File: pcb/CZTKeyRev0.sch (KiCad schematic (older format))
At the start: 195 parts, among them U1 proton_c

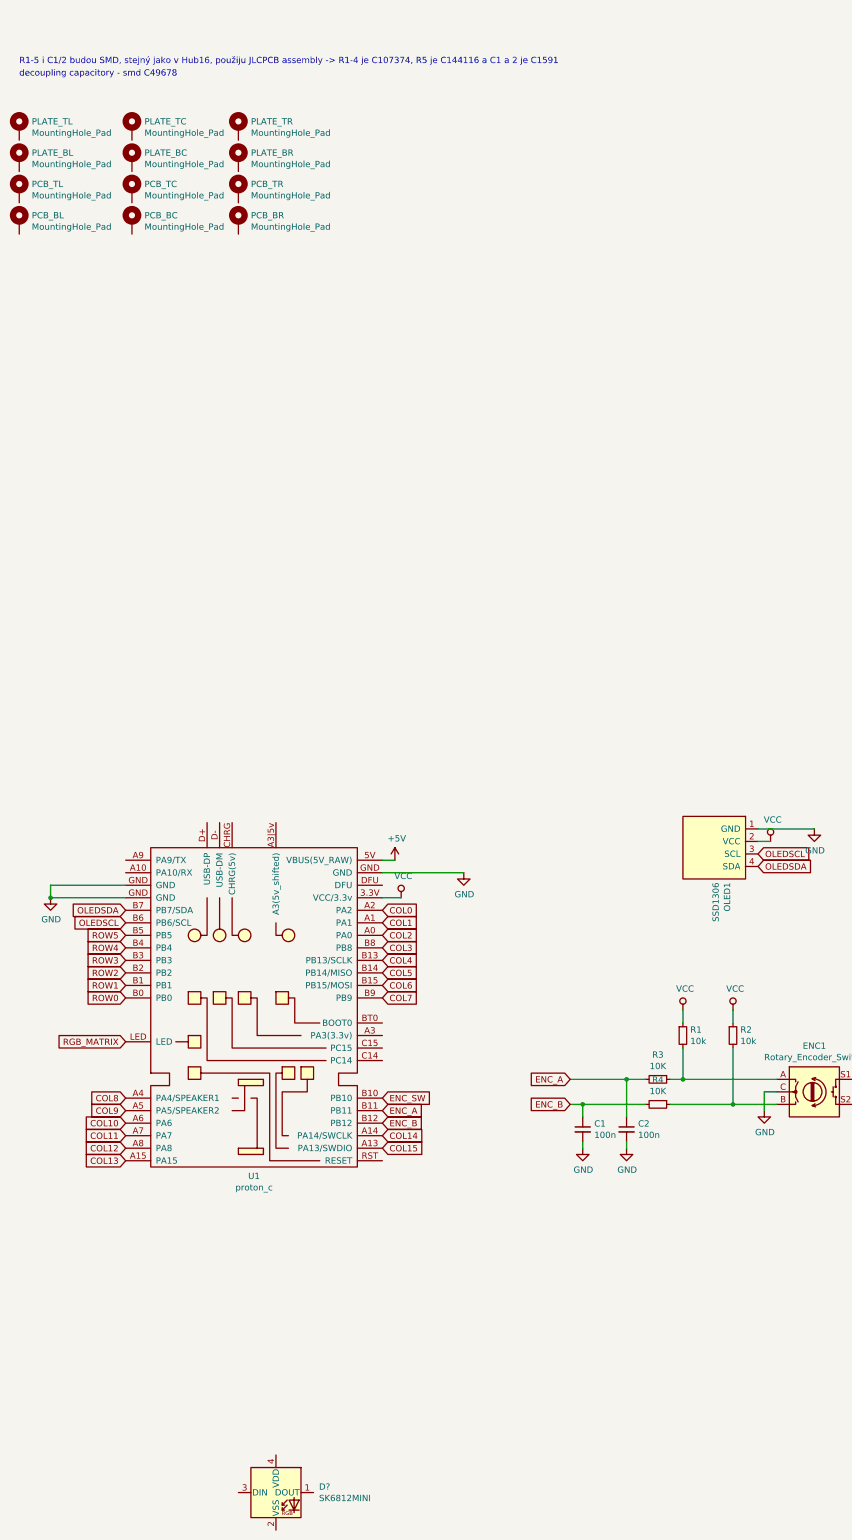
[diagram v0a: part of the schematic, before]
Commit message: Added the IC for ext 5v and led data
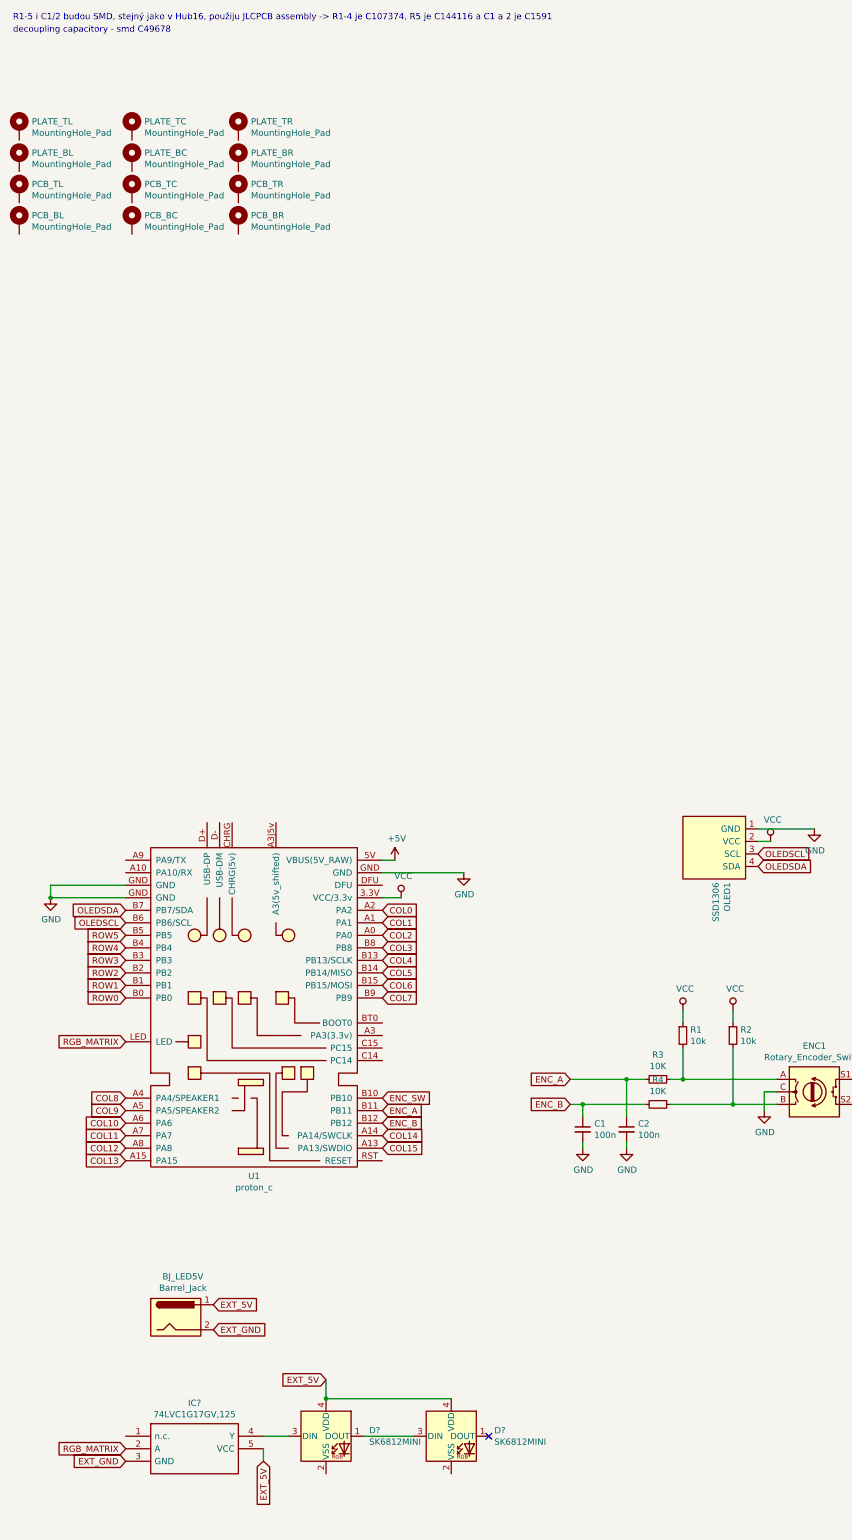
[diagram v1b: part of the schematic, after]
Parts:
- added BJ_LED5V: Barrel_Jack, symbol Connector:Barrel_Jack
- added D?: SK6812MINI, LED_SMD:LED_SK6812MINI_PLCC4_3.5x3.5mm_P1.75mm, symbol LED:SK6812MINI
- added IC?: 74LVC1G17GV,125, SOT95P275X110-5N, symbol SamacSys_Parts:74LVC1G17GV,125
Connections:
- net RGB_MATRIX: now also IC?.2 (A)
- net at D?.1 (DOUT): now also D?.3 (DIN)
- net at D?.3 (DIN): now also IC?.4 (Y)
- net EXT_5V: now reaches D?.4 (VDD)
- net EXT_5V: now also BJ_LED5V.1, D?.4 (VDD), IC?.5 (VCC)
- new net EXT_GND: BJ_LED5V.2, IC?.3 (GND)
- no-connect marks 0 -> 1
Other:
- moved on the sheet: D?
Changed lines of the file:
@@
 Text GLabel 1450 7950 0    50   Input ~ 0
 RGB_MATRIX
-Text Notes 600  150  0    50   ~ 0
+Text Notes 550  -200 0    50   ~ 0
 R1-5 i C1/2 budou SMD, stejný jako v Hub16, použiju JLCPCB assembly -> R1-4 je C107374, R5 je C144116 a C1 a 2 je C1591
 Text GLabel 3500 8500 2    50   Input ~ 0
@@
 Text GLabel 12200 9150 2    50   Input ~ 0
 ENC_S2
-Text Notes 600  250  0    50   ~ 0
+Text Notes 550  -100 0    50   ~ 0
 decoupling capacitory - smd C49678
 Wire Wire Line
@@
 $EndComp
 $Comp
+L Connector:Barrel_Jack BJ_LED5V
+U 1 1 5FC7DC4D
+P 1850 10150
+F 0 "BJ_LED5V" H 1907 10475 50  0000 C CNN
+F 1 "Barrel_Jack" H 1907 10384 50  0000 C CNN
+F 2 "" H 1900 10110 50  0001 C CNN
+F 3 "~" H 1900 10110 50  0001 C CNN
+	1    1850 10150
+	1    0    0    -1
+$EndComp
+Text GLabel 1450 11200 0    50   Input ~ 0
+RGB_MATRIX
+$Comp
+L LED:SK6812MINI D?
+U 1 1 5FC81A59
+P 4050 11100
+F 0 "D?" H 4394 11146 50  0000 L CNN
+F 1 "SK6812MINI" H 4394 11055 50  0000 L CNN
+F 2 "LED_SMD:LED_SK6812MINI_PLCC4_3.5x3.5mm_P1.75mm" H 4100 10800 50  0001 L TNN
+F 3 "https://cdn-shop.adafruit.com/product-files/2686/SK6812MINI_REV.01-1-2.pdf" H 4150 10725 50  0001 L TNN
+	1    4050 11100
+	1    0    0    -1
+$EndComp
+NoConn ~ 4350 11100
+Text GLabel 2150 10050 2    50   Input ~ 0
+EXT_5V
+Text GLabel 2150 10250 2    50   Input ~ 0
+EXT_GND
+Text GLabel 1450 11300 0    50   Input ~ 0
+EXT_GND
+Text GLabel 2550 11300 3    50   Input ~ 0
+EXT_5V
+$Comp
 L LED:SK6812MINI D?
 U 1 1 5FCBCA87
-P 2650 11550
-F 0 "D?" H 2994 11596 50  0000 L CNN
-F 1 "SK6812MINI" H 2994 11505 50  0000 L CNN
-F 2 "LED_SMD:LED_SK6812MINI_PLCC4_3.5x3.5mm_P1.75mm" H 2700 11250 50  0001 L TNN
-F 3 "https://cdn-shop.adafruit.com/product-files/2686/SK6812MINI_REV.01-1-2.pdf" H 2750 11175 50  0001 L TNN
-	1    2650 11550
-	1    0    0    -1
-$EndComp
+P 3050 11100
+F 0 "D?" H 3394 11146 50  0000 L CNN
+F 1 "SK6812MINI" H 3394 11055 50  0000 L CNN
+F 2 "LED_SMD:LED_SK6812MINI_PLCC4_3.5x3.5mm_P1.75mm" H 3100 10800 50  0001 L TNN
+F 3 "https://cdn-shop.adafruit.com/product-files/2686/SK6812MINI_REV.01-1-2.pdf" H 3150 10725 50  0001 L TNN
+	1    3050 11100
+	1    0    0    -1
+$EndComp
+$Comp
+L SamacSys_Parts:74LVC1G17GV,125 IC?
+U 1 1 5FEEF888
+P 1450 11100
+F 0 "IC?" H 2000 11365 50  0000 C CNN
+F 1 "74LVC1G17GV,125" H 2000 11274 50  0000 C CNN
+F 2 "SOT95P275X110-5N" H 2400 11200 50  0001 L CNN
+F 3 "https://assets.nexperia.com/documents/data-sheet/74LVC1G17.pdf" H 2400 11100 50  0001 L CNN
+F 4 "74LVC1G17 - Single Schmitt trigger buffer@en-us" H 2400 11000 50  0001 L CNN "Description"
+F 5 "1.1" H 2400 10900 50  0001 L CNN "Height"
+F 6 "771-LVC1G17GV125" H 2400 10800 50  0001 L CNN "Mouser Part Number"
+F 7 "https://www.mouser.co.uk/ProductDetail/Nexperia/74LVC1G17GV125?qs=me8TqzrmIYX3DxU5Fpa8sQ%3D%3D" H 2400 10700 50  0001 L CNN "Mouser Price/Stock"
+F 8 "Nexperia" H 2400 10600 50  0001 L CNN "Manufacturer_Name"
+F 9 "74LVC1G17GV,125" H 2400 10500 50  0001 L CNN "Manufacturer_Part_Number"
+	1    1450 11100
+	1    0    0    -1
+$EndComp
+Wire Wire Line
+	2550 11100 2750 11100
+Wire Wire Line
+	2550 11200 2550 11300
+Wire Wire Line
+	3350 11100 3750 11100
+Text GLabel 3050 10650 0    50   Input ~ 0
+EXT_5V
+Wire Wire Line
+	3050 10650 3050 10800
+Wire Wire Line
+	4050 10800 3050 10800
+Connection ~ 3050 10800
 $EndSCHEMATC

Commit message: Organizing lib, gerber and schematic pdf files into subfolders
Its for easier navigation
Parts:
- removed C1, C2: 100n, Capacitor_SMD:C_0603_1608Metric, symbol Device:C_Small
- removed D? (x2): SK6812MINI, LED_SMD:LED_SK6812MINI_PLCC4_3.5x3.5mm_P1.75mm, symbol LED:SK6812MINI
- removed R1, R2: 10k, Resistor_SMD:R_Array_Convex_4x0603, symbol Device:R_Small
- removed R3, R4: 10K, Resistor_SMD:R_Array_Convex_4x0603, symbol Device:R_Small
- added LED1, LED10, LED11, LED12, LED13, LED14, LED15, LED16, LED17, LED18, LED19, LED2, LED20, LED21, LED22, LED23, LED24, LED25, LED26, LED27, LED28, LED29, LED3, LED30, LED31, LED32, LED33, LED34, LED35, LED36, LED37, LED38, LED39, LED4, LED40, LED41, LED42, LED43, LED44, LED45, LED46, LED47, LED48, LED49, LED5, LED50, LED51, LED52, LED53, LED54, LED55, LED56, LED57, LED58, LED59, LED6, LED60, LED61, LED62, LED63, LED64, LED65, LED66, LED67, LED68, LED69, LED7, LED70, LED71, LED72, LED73, LED74, LED75, LED76, LED77, LED78, LED79, LED8, LED80, LED81, LED82, LED83, LED84, LED85, LED86, LED87, LED9: YS-SK6812MINI-E, rgb led reverse mount:SK6812MINIE-simple, symbol kbd:YS-SK6812MINI-E
- EXT_IC1: renamed from IC?; footprint SOT95P275X110-5N -> SamacSys_Parts:SOT95P275X110-5N
- PCB_BC1: renamed from PCB_BC; footprint (none) -> MountingHole:MountingHole_2.2mm_M2_Pad
- PCB_BL1: renamed from PCB_BL; footprint (none) -> MountingHole:MountingHole_2.2mm_M2_Pad
- PCB_BR1: renamed from PCB_BR; footprint (none) -> MountingHole:MountingHole_2.2mm_M2_Pad
- PCB_TC1: renamed from PCB_TC; footprint (none) -> MountingHole:MountingHole_2.2mm_M2_Pad
- PCB_TL1: renamed from PCB_TL; footprint (none) -> MountingHole:MountingHole_2.2mm_M2_Pad
- PCB_TR1: renamed from PCB_TR; footprint (none) -> MountingHole:MountingHole_2.2mm_M2_Pad
- PLATE_BC1: renamed from PLATE_BC; footprint (none) -> MountingHole:MountingHole_2.2mm_M2_Pad
- PLATE_BL1: renamed from PLATE_BL; footprint (none) -> MountingHole:MountingHole_2.2mm_M2_Pad
- PLATE_BR1: renamed from PLATE_BR; footprint (none) -> MountingHole:MountingHole_2.2mm_M2_Pad
- PLATE_TC1: renamed from PLATE_TC; footprint (none) -> MountingHole:MountingHole_2.2mm_M2_Pad
- PLATE_TL1: renamed from PLATE_TL; footprint (none) -> MountingHole:MountingHole_2.2mm_M2_Pad
- PLATE_TR1: renamed from PLATE_TR; footprint (none) -> MountingHole:MountingHole_2.2mm_M2_Pad
- renumbered BJ_LED5V to BJ_LED5V1, D87 to D0
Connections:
- net +5V: now also OLED1.2 (VCC)
- net COL0: now also ENC1.S1
- net COL4: no longer ENC1.S1
- net ENC_A: now also ENC1.A
- net ENC_B: now also ENC1.B
- net EXT_5V: now also LED1.1 (VDD), LED10.1 (VDD), LED11.1 (VDD), LED12.1 (VDD), LED13.1 (VDD), LED14.1 (VDD), LED15.1 (VDD), LED16.1 (VDD), LED17.1 (VDD), LED18.1 (VDD), LED19.1 (VDD), LED2.1 (VDD), LED20.1 (VDD), LED21.1 (VDD), LED22.1 (VDD), LED23.1 (VDD), LED24.1 (VDD), LED25.1 (VDD), LED26.1 (VDD), LED27.1 (VDD), LED28.1 (VDD), LED29.1 (VDD), LED3.1 (VDD), LED30.1 (VDD), LED31.1 (VDD), LED32.1 (VDD), LED33.1 (VDD), LED34.1 (VDD), LED35.1 (VDD), LED36.1 (VDD), LED37.1 (VDD), LED38.1 (VDD), LED39.1 (VDD), LED4.1 (VDD), LED40.1 (VDD), LED41.1 (VDD), LED42.1 (VDD), LED43.1 (VDD), LED44.1 (VDD), LED45.1 (VDD), LED46.1 (VDD), LED47.1 (VDD), LED48.1 (VDD), LED49.1 (VDD), LED5.1 (VDD), LED50.1 (VDD), LED51.1 (VDD), LED52.1 (VDD), LED53.1 (VDD), LED54.1 (VDD), LED55.1 (VDD), LED56.1 (VDD), LED57.1 (VDD), LED58.1 (VDD), LED59.1 (VDD), LED6.1 (VDD), LED60.1 (VDD), LED61.1 (VDD), LED62.1 (VDD), LED63.1 (VDD), LED64.1 (VDD), LED65.1 (VDD), LED66.1 (VDD), LED67.1 (VDD), LED68.1 (VDD), LED69.1 (VDD), LED7.1 (VDD), LED70.1 (VDD), LED71.1 (VDD), LED72.1 (VDD), LED73.1 (VDD), LED74.1 (VDD), LED75.1 (VDD), LED76.1 (VDD), LED77.1 (VDD), LED78.1 (VDD), LED79.1 (VDD), LED8.1 (VDD), LED80.1 (VDD), LED81.1 (VDD), LED82.1 (VDD), LED83.1 (VDD), LED84.1 (VDD), LED85.1 (VDD), LED86.1 (VDD), LED87.1 (VDD), LED9.1 (VDD)
- net EXT_GND: now also LED1.3 (VSS), LED10.3 (VSS), LED11.3 (VSS), LED12.3 (VSS), LED13.3 (VSS), LED14.3 (VSS), LED15.3 (VSS), LED16.3 (VSS), LED17.3 (VSS), LED18.3 (VSS), LED19.3 (VSS), LED2.3 (VSS), LED20.3 (VSS), LED21.3 (VSS), LED22.3 (VSS), LED23.3 (VSS), LED24.3 (VSS), LED25.3 (VSS), LED26.3 (VSS), LED27.3 (VSS), LED28.3 (VSS), LED29.3 (VSS), LED3.3 (VSS), LED30.3 (VSS), LED31.3 (VSS), LED32.3 (VSS), LED33.3 (VSS), LED34.3 (VSS), LED35.3 (VSS), LED36.3 (VSS), LED37.3 (VSS), LED38.3 (VSS), LED39.3 (VSS), LED4.3 (VSS), LED40.3 (VSS), LED41.3 (VSS), LED42.3 (VSS), LED43.3 (VSS), LED44.3 (VSS), LED45.3 (VSS), LED46.3 (VSS), LED47.3 (VSS), LED48.3 (VSS), LED49.3 (VSS), LED5.3 (VSS), LED50.3 (VSS), LED51.3 (VSS), LED52.3 (VSS), LED53.3 (VSS), LED54.3 (VSS), LED55.3 (VSS), LED56.3 (VSS), LED57.3 (VSS), LED58.3 (VSS), LED59.3 (VSS), LED6.3 (VSS), LED60.3 (VSS), LED61.3 (VSS), LED62.3 (VSS), LED63.3 (VSS), LED64.3 (VSS), LED65.3 (VSS), LED66.3 (VSS), LED67.3 (VSS), LED68.3 (VSS), LED69.3 (VSS), LED7.3 (VSS), LED70.3 (VSS), LED71.3 (VSS), LED72.3 (VSS), LED73.3 (VSS), LED74.3 (VSS), LED75.3 (VSS), LED76.3 (VSS), LED77.3 (VSS), LED78.3 (VSS), LED79.3 (VSS), LED8.3 (VSS), LED80.3 (VSS), LED81.3 (VSS), LED82.3 (VSS), LED83.3 (VSS), LED84.3 (VSS), LED85.3 (VSS), LED86.3 (VSS), LED87.3 (VSS), LED9.3 (VSS)
- net ROW0: now also D0.1 (K)
- net ROW5: no longer D0.1 (K)
- net VCC: no longer OLED1.2 (VCC)
- net at EXT_IC1.4 (Y): now also LED1.4 (DIN)
- net ENC_SW: no longer names the net of U1.B10 (PB10)
- new net: LED1.2 (DOUT), LED2.4 (DIN)
- new net: LED2.2 (DOUT), LED3.4 (DIN)
- new net: LED3.2 (DOUT), LED4.4 (DIN)
- new net: LED4.2 (DOUT), LED5.4 (DIN)
- new net: LED5.2 (DOUT), LED6.4 (DIN)
- new net: LED6.2 (DOUT), LED7.4 (DIN)
- new net: LED7.2 (DOUT), LED8.4 (DIN)
- new net: LED8.2 (DOUT), LED9.4 (DIN)
- new net: LED10.4 (DIN), LED9.2 (DOUT)
- new net: LED10.2 (DOUT), LED11.4 (DIN)
- new net: LED11.2 (DOUT), LED12.4 (DIN)
- new net: LED12.2 (DOUT), LED13.4 (DIN)
- new net: LED13.2 (DOUT), LED14.4 (DIN)
- new net: LED14.2 (DOUT), LED30.4 (DIN)
- new net: LED29.4 (DIN), LED30.2 (DOUT)
- new net: LED28.4 (DIN), LED29.2 (DOUT)
- new net: LED27.4 (DIN), LED28.2 (DOUT)
- new net: LED26.4 (DIN), LED27.2 (DOUT)
- new net: LED25.4 (DIN), LED26.2 (DOUT)
- new net: LED24.4 (DIN), LED25.2 (DOUT)
- new net: LED23.4 (DIN), LED24.2 (DOUT)
- new net: LED22.4 (DIN), LED23.2 (DOUT)
- new net: LED21.4 (DIN), LED22.2 (DOUT)
- new net: LED20.4 (DIN), LED21.2 (DOUT)
- new net: LED19.4 (DIN), LED20.2 (DOUT)
- new net: LED18.4 (DIN), LED19.2 (DOUT)
- new net: LED17.4 (DIN), LED18.2 (DOUT)
- new net: LED16.4 (DIN), LED17.2 (DOUT)
- new net: LED15.4 (DIN), LED16.2 (DOUT)
- new net: LED15.2 (DOUT), LED31.4 (DIN)
- new net: LED31.2 (DOUT), LED32.4 (DIN)
- new net: LED32.2 (DOUT), LED33.4 (DIN)
- new net: LED33.2 (DOUT), LED34.4 (DIN)
- new net: LED34.2 (DOUT), LED35.4 (DIN)
- new net: LED35.2 (DOUT), LED36.4 (DIN)
- new net: LED36.2 (DOUT), LED37.4 (DIN)
- new net: LED37.2 (DOUT), LED38.4 (DIN)
- new net: LED38.2 (DOUT), LED39.4 (DIN)
- new net: LED39.2 (DOUT), LED40.4 (DIN)
- new net: LED40.2 (DOUT), LED41.4 (DIN)
- new net: LED41.2 (DOUT), LED42.4 (DIN)
- new net: LED42.2 (DOUT), LED43.4 (DIN)
- new net: LED43.2 (DOUT), LED44.4 (DIN)
- new net: LED44.2 (DOUT), LED45.4 (DIN)
- new net: LED45.2 (DOUT), LED46.4 (DIN)
- new net: LED46.2 (DOUT), LED61.4 (DIN)
- new net: LED60.4 (DIN), LED61.2 (DOUT)
- new net: LED59.4 (DIN), LED60.2 (DOUT)
- new net: LED58.4 (DIN), LED59.2 (DOUT)
- new net: LED57.4 (DIN), LED58.2 (DOUT)
- new net: LED56.4 (DIN), LED57.2 (DOUT)
- new net: LED55.4 (DIN), LED56.2 (DOUT)
- new net: LED54.4 (DIN), LED55.2 (DOUT)
- new net: LED53.4 (DIN), LED54.2 (DOUT)
- new net: LED52.4 (DIN), LED53.2 (DOUT)
- new net: LED51.4 (DIN), LED52.2 (DOUT)
- new net: LED50.4 (DIN), LED51.2 (DOUT)
- new net: LED49.4 (DIN), LED50.2 (DOUT)
- new net: LED48.4 (DIN), LED49.2 (DOUT)
- new net: LED47.4 (DIN), LED48.2 (DOUT)
- new net: LED47.2 (DOUT), LED62.4 (DIN)
- new net: LED76.2 (DOUT), LED87.4 (DIN)
- new net: LED75.2 (DOUT), LED76.4 (DIN)
- new net: LED74.2 (DOUT), LED75.4 (DIN)
- new net: LED73.2 (DOUT), LED74.4 (DIN)
- new net: LED72.2 (DOUT), LED73.4 (DIN)
- new net: LED71.2 (DOUT), LED72.4 (DIN)
- new net: LED70.2 (DOUT), LED71.4 (DIN)
- new net: LED69.2 (DOUT), LED70.4 (DIN)
- new net: LED68.2 (DOUT), LED69.4 (DIN)
- new net: LED67.2 (DOUT), LED68.4 (DIN)
- new net: LED66.2 (DOUT), LED67.4 (DIN)
- new net: LED65.2 (DOUT), LED66.4 (DIN)
- new net: LED64.2 (DOUT), LED65.4 (DIN)
- new net: LED63.2 (DOUT), LED64.4 (DIN)
- new net: LED62.2 (DOUT), LED63.4 (DIN)
- new net: LED86.4 (DIN), LED87.2 (DOUT)
- new net: LED85.4 (DIN), LED86.2 (DOUT)
- new net: LED84.4 (DIN), LED85.2 (DOUT)
- new net: LED83.4 (DIN), LED84.2 (DOUT)
- new net: LED82.4 (DIN), LED83.2 (DOUT)
- new net: LED81.4 (DIN), LED82.2 (DOUT)
- new net: LED79.4 (DIN), LED80.2 (DOUT)
- new net: LED80.4 (DIN), LED81.2 (DOUT)
- new net: LED78.4 (DIN), LED79.2 (DOUT)
- new net: LED77.4 (DIN), LED78.2 (DOUT)
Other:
- note added: "EXTERNAL POWER SUPPLY"
- note added: "MCU\n"
- note added: "MOUNTING HOLES\n"
- note added: "OLED"
- note added: "ROTARY ENCODER\n"
- note added: "SK6812MINI-E MATRIX\nincludes the 74LVC1G17GV,125"
- note added: "SWITCH MATRIX"
- note removed: "R1-5 i C1/2 budou SMD, stejný jako v Hub16, použiju JLCPCB assembly -> R1-4 je C107374, R5 je C144116 a C1 a 2 je C1591"
- note removed: "decoupling capacitory - smd C49678"
- moved on the sheet: BJ_LED5V1, D0, D1, D10, D11, D12, D13, D14, D15, D16, D17, D18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

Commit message: Resistor between MCU and DIN of SK6812MINI-E
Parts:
- removed BJ_LED5V1: Barrel_Jack, symbol Connector:Barrel_Jack
- added BJ_LED5V1: Barrel_Jack_Switch, symbol Connector:Barrel_Jack_Switch
- added DC1, DC? (x86): 100n, symbol Device:C_Small
- added R?: 300-500 - C422828, symbol Device:R_Small
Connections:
- net EXT_GND is gone; now on net GND: EXT_IC1.3 (GND), LED1.3 (VSS), LED10.3 (VSS), LED11.3 (VSS), LED12.3 (VSS), LED13.3 (VSS), LED14.3 (VSS), LED15.3 (VSS), LED16.3 (VSS), LED17.3 (VSS), LED18.3 (VSS), LED19.3 (VSS), LED2.3 (VSS), LED20.3 (VSS), LED21.3 (VSS), LED22.3 (VSS), LED23.3 (VSS), LED24.3 (VSS), LED25.3 (VSS), LED26.3 (VSS), LED27.3 (VSS), LED28.3 (VSS), LED29.3 (VSS), LED3.3 (VSS), LED30.3 (VSS), LED31.3 (VSS), LED32.3 (VSS), LED33.3 (VSS), LED34.3 (VSS), LED35.3 (VSS), LED36.3 (VSS), LED37.3 (VSS), LED38.3 (VSS), LED39.3 (VSS), LED4.3 (VSS), LED40.3 (VSS), LED41.3 (VSS), LED42.3 (VSS), LED43.3 (VSS), LED44.3 (VSS), LED45.3 (VSS), LED46.3 (VSS), LED47.3 (VSS), LED48.3 (VSS), LED49.3 (VSS), LED5.3 (VSS), LED50.3 (VSS), LED51.3 (VSS), LED52.3 (VSS), LED53.3 (VSS), LED54.3 (VSS), LED55.3 (VSS), LED56.3 (VSS), LED57.3 (VSS), LED58.3 (VSS), LED59.3 (VSS), LED6.3 (VSS), LED60.3 (VSS), LED61.3 (VSS), LED62.3 (VSS), LED63.3 (VSS), LED64.3 (VSS), LED65.3 (VSS), LED66.3 (VSS), LED67.3 (VSS), LED68.3 (VSS), LED69.3 (VSS), LED7.3 (VSS), LED70.3 (VSS), LED71.3 (VSS), LED72.3 (VSS), LED73.3 (VSS), LED74.3 (VSS), LED75.3 (VSS), LED76.3 (VSS), LED77.3 (VSS), LED78.3 (VSS), LED79.3 (VSS), LED8.3 (VSS), LED80.3 (VSS), LED81.3 (VSS), LED82.3 (VSS), LED83.3 (VSS), LED84.3 (VSS), LED85.3 (VSS), LED86.3 (VSS), LED87.3 (VSS), LED9.3 (VSS)
- net EXT_5V: now also BJ_LED5V1.1, DC1.2, DC?.1, DC?.1, DC?.1, DC?.1, DC?.1, DC?.1, DC?.1, DC?.1, DC?.1, DC?.1, DC?.1, DC?.1, DC?.1, DC?.2, DC?.2, DC?.2, DC?.2, DC?.2, DC?.2, DC?.2, DC?.2, DC?.2, DC?.2, DC?.2, DC?.2, DC?.2, DC?.2, DC?.2, DC?.2, DC?.2, DC?.2, DC?.2, DC?.2, DC?.2, DC?.2, DC?.2, DC?.2, DC?.2, DC?.2, DC?.2, DC?.2, DC?.2, DC?.2, DC?.2, DC?.2, DC?.2, DC?.2, DC?.2, DC?.2, DC?.2, DC?.2, DC?.2, DC?.2, DC?.2, DC?.2, DC?.2, DC?.2, DC?.2, DC?.2, DC?.2, DC?.2, DC?.2, DC?.2, DC?.2, DC?.2, DC?.2, DC?.2, DC?.2, DC?.2, DC?.2, DC?.2, DC?.2, DC?.2, DC?.2, DC?.2, DC?.2, DC?.2, DC?.2, DC?.2, DC?.2, DC?.2, DC?.2, DC?.2, DC?.2, DC?.2, DC?.2
- net GND: now also BJ_LED5V1.2, DC1.1, DC?.1, DC?.1, DC?.1, DC?.1, DC?.1, DC?.1, DC?.1, DC?.1, DC?.1, DC?.1, DC?.1, DC?.1, DC?.1, DC?.1, DC?.1, DC?.1, DC?.1, DC?.1, DC?.1, DC?.1, DC?.1, DC?.1, DC?.1, DC?.1, DC?.1, DC?.1, DC?.1, DC?.1, DC?.1, DC?.1, DC?.1, DC?.1, DC?.1, DC?.1, DC?.1, DC?.1, DC?.1, DC?.1, DC?.1, DC?.1, DC?.1, DC?.1, DC?.1, DC?.1, DC?.1, DC?.1, DC?.1, DC?.1, DC?.1, DC?.1, DC?.1, DC?.1, DC?.1, DC?.1, DC?.1, DC?.1, DC?.1, DC?.1, DC?.1, DC?.1, DC?.1, DC?.1, DC?.1, DC?.1, DC?.1, DC?.1, DC?.1, DC?.1, DC?.1, DC?.1, DC?.1, DC?.1, DC?.1, DC?.2, DC?.2, DC?.2, DC?.2, DC?.2, DC?.2, DC?.2, DC?.2, DC?.2, DC?.2, DC?.2, DC?.2, DC?.2
- net RGB_MATRIX: now also R?.2; no longer U1.LED
- new net: R?.1, U1.LED

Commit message: Added footprint to the resistor
0805 Hand Solder. Altough this is going to be using SMT assembly from jlcpcb I wanted to add an option to see what would happen if it was a 0ohm resistor istead....
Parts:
- R1: renamed from R?; footprint (none) -> Resistor_SMD:R_0805_2012Metric_Pad1.15x1.40mm_HandSolder
- gave numbers to parts that had none: 86

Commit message: Hopefully final touches
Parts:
- removed DC77: 100n, symbol Device:C_Small
- removed LED77: YS-SK6812MINI-E, rgb led reverse mount:SK6812MINIE-simple, symbol kbd:YS-SK6812MINI-E
- added PCB_MC1: MountingHole_Pad, MountingHole:MountingHole_2.2mm_M2_Pad, symbol Mechanical:MountingHole_Pad
- BJ_LED5V1: footprint (none) -> rgb led reverse mount:BarrelJackP1
- DC1, DC10, DC11, DC12, DC13, DC14, DC15, DC16, DC17, DC18, DC19, DC2, DC20, DC21, DC22, DC23, DC24, DC25, DC26, DC27, DC28, DC29, DC3, DC30, DC31, DC32, DC33, DC34, DC35, DC36, DC37, DC38, DC39, DC4, DC40, DC41, DC42, DC43, DC44, DC45, DC46, DC47, DC48, DC49, DC5, DC50, DC51, DC52, DC53, DC54, DC55, DC56, DC57, DC58, DC59, DC6, DC60, DC61, DC62, DC63, DC64, DC65, DC66, DC67, DC68, DC69, DC7, DC70, DC71, DC72, DC73, DC74, DC75, DC76, DC78, DC79, DC8, DC80, DC81, DC82, DC83, DC84, DC85, DC86, DC87, DC9: footprint (none) -> Capacitor_SMD:C_0805_2012Metric_Pad1.15x1.40mm_HandSolder
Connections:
- net RGB_MATRIX: now also R1.1; no longer R1.2
- net at U1.B10 (PB10): now also R1.2
- net at U1.LED: no longer R1.1
- no-connect marks 1 -> 0
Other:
- note added: "DecouplingCapacitors - C49678 (0805)\n"
- moved on the sheet: R1
